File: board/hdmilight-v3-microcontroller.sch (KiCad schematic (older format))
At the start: 11 parts, among them SW1 SW_Push, SW2 SW_Push, U1 STM32F303RETx

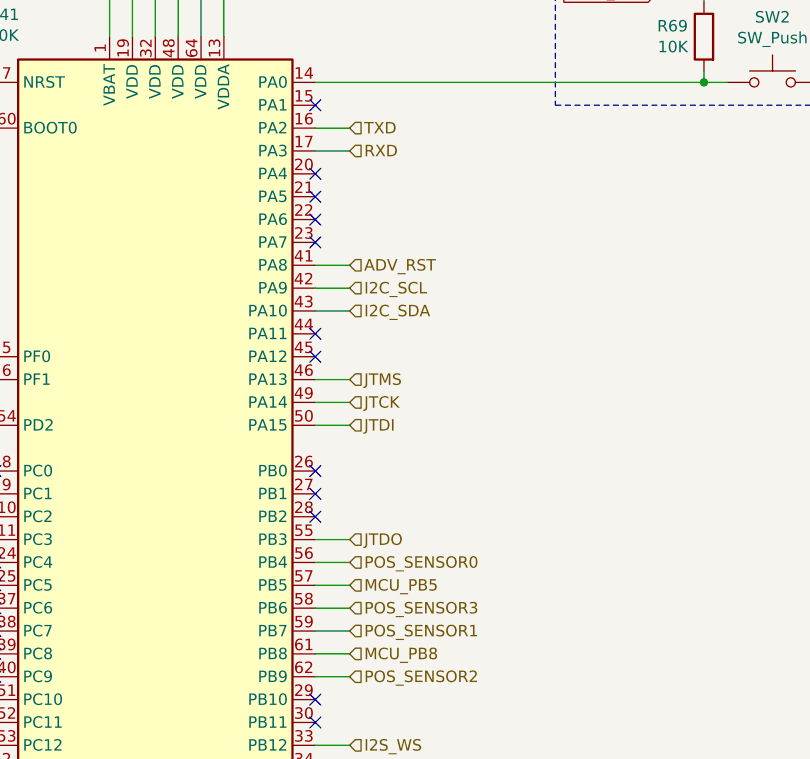
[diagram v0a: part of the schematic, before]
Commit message: Fixed bugs in v3.0 board:
 * Changed FPGA GPIO to 2 row with ground to make it compatible with logic analyser plug for debugging
 * Move position sensor from PB4 to PB5
 * Connect voltage regulator center pad to ground pins
 * Add SPI CS line between FPGA and MCU
 * Move HDMI hotplug LED back from board edge
 * Move HDMI ESD chip closer to connector
 * Swap serial rx/tx
 * Fix FPGA EEPROM footprint
 * Fix reset button footprint
 * Connect ADV I2C to MCU
 * Fix missing ground to hotplug power off circuit
 * Move LED power connector to back of board
 * Move standby button to front of board
 * Only use HDMI 5v for hotplug detect
 * Change LED power switching to high side to stop it grounding back through the data line
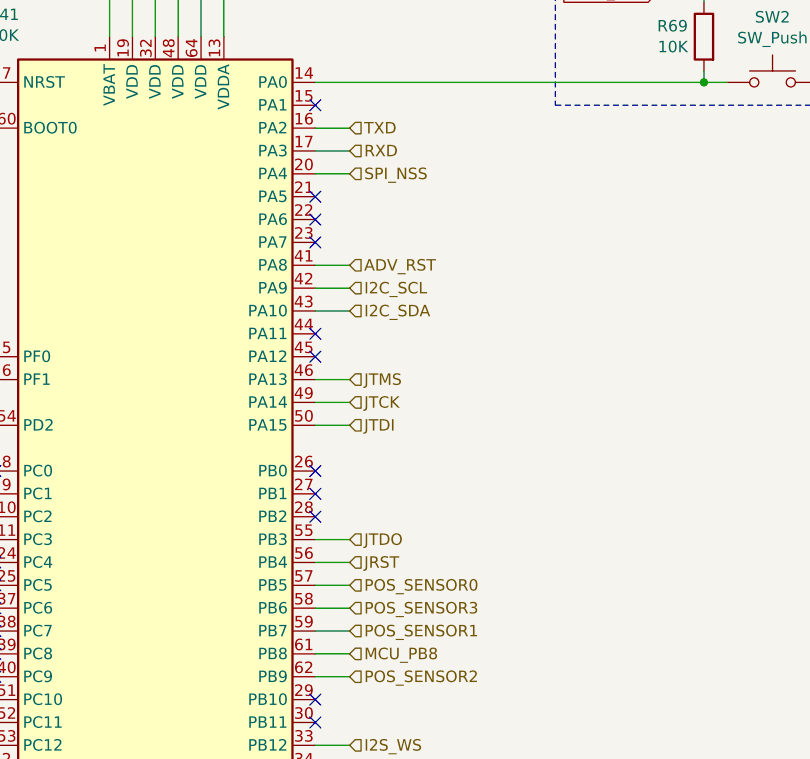
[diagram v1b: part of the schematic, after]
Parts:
- SW1: footprint Button_Switch_SMD:SW_SPST_B3S-1000 -> Button_Switch_SMD:SW_SPST_EVQP0
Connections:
- net MCU_PB5 is gone; now on net POS_SENSOR0: U1.57 (PB5)
- net POS_SENSOR0: no longer U1.56 (PB4)
- net SPI_NSS: now reaches U1.20 (PA4)
- new net JRST: U1.56 (PB4)
- no-connect marks 20 -> 19
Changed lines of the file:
@@
 $Descr A4 11693 8268
 encoding utf-8
-Sheet 8 8
+Sheet 7 8
 Title "HDMI Light V3 - Microcontroller"
 Date "2019-10-29"
@@
 Wire Wire Line
 	3950 2400 4100 2400
-Text HLabel 4100 4200 2    50   Input ~ 0
-POS_SENSOR0
 Text HLabel 4100 4500 2    50   Input ~ 0
 POS_SENSOR1
@@
 Wire Wire Line
 	2450 3600 2550 3600
-Text HLabel 4100 4300 2    50   Input ~ 0
-MCU_PB5
 Text HLabel 4100 4600 2    50   Input ~ 0
 MCU_PB8
@@
 F 0 "SW1" H 2150 2385 50  0000 C CNN
 F 1 "SW_Push" H 2150 2294 50  0000 C CNN
-F 2 "Button_Switch_SMD:SW_SPST_B3S-1000" H 2150 2300 50  0001 C CNN
+F 2 "Button_Switch_SMD:SW_SPST_EVQP0" H 2150 2300 50  0001 C CNN
 F 3 "~" H 2150 2300 50  0001 C CNN
 	1    2150 2100
@@
 NoConn ~ 3950 2700
 NoConn ~ 3950 2600
-NoConn ~ 3950 2500
 NoConn ~ 3950 2200
 NoConn ~ 2550 4200
@@
 $EndComp
 NoConn ~ 2550 3800
+Wire Wire Line
+	3950 2500 4100 2500
+Text HLabel 4100 2500 2    50   Input ~ 0
+SPI_NSS
+Text HLabel 4100 4300 2    50   Input ~ 0
+POS_SENSOR0
+Text HLabel 4100 4200 2    50   Input ~ 0
+JRST
 $EndSCHEMATC
